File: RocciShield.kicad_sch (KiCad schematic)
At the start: 117 parts, among them J1 Battery, J2 M1, J3 M1, J4 M1, J5 M1, U1 DRV8871DDA, U2 TL7712A, U3 LMR33630CDDA, U4 DRV8871DDA, U5 DRV8871DDA, U6 DRV8871DDA, U7 TCA9548APWR, U8 AMS1117-3.3

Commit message: fixed issue #1 and some more things
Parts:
- removed C4: 22 µF, symbol Device:C
- removed D10: GR, symbol Device:LED
- removed R16: 430, symbol Device:R
- removed U2: TL7712A, symbol Power_Supervisor:TL7712A
- added C12, C18, C6: 100n, symbol Device:C
- added C4, C5: 22 µF, symbol Device:C_Polarized
- added D17: RED, symbol Device:LED
- added D6, D7, D8: GR, symbol Device:LED
- added F1, F11, F14, F17, F20, F23, F5, F8: 100 mA, symbol Device:Polyfuse
- added F26: 3A, symbol Device:Polyfuse
- added F27: 1A, symbol Device:Polyfuse
- added J11: I2C6, symbol Connector:Conn_01x04_Pin
- added J13: I2C7, symbol Connector:Conn_01x04_Pin
- added J14: Power, symbol Connector:Conn_01x04_Socket
- added J2: I2C0, symbol Connector:Conn_01x04_Pin
- added J3: I2C1, symbol Connector:Conn_01x04_Pin
- added J4: I2C2, symbol Connector:Conn_01x04_Pin
- added J5: I2C3, symbol Connector:Conn_01x04_Pin
- added J7: I2C4, symbol Connector:Conn_01x04_Pin
- added J9: I2C5, symbol Connector:Conn_01x04_Pin
- added Q1: IRF7416, symbol Device:Q_PMOS_GDS
- added R10: 383k 1%, symbol Device:R
- added R11: 10k, symbol Device:R
- added R12: 200, symbol Device:R
- added R13, R28: 20, symbol Device:R
- added R14: 1k, symbol Device:R
- added R15: 1k47 1%, symbol Device:R
- added R18: 14k3 1%, symbol Device:R
- added TP1, TP10, TP11, TP12, TP13, TP14, TP15, TP16, TP17, TP18, TP19, TP2, TP20, TP21, TP22, TP3, TP4, TP5, TP6, TP7, TP8, TP9: ~, symbol Connector:TestPoint
- added U3: L7808, symbol Regulator_Linear:L7808
- added U4: TPS3700, SOT95P280X110-6N, symbol TPS3700DDCR:TPS3700DDCR
- C11: value 22 µF -> 100n
- J10: renamed from J4; value M1 -> M3
- J12: renamed from J5; value M1 -> M4
- J8: renamed from J3; value M1 -> M2
- R21: renamed from R5; value 430 -> 1k
- R22: renamed from R6; value 430 -> 1k
- R26: renamed from R8; value 430 -> 1k
- R27: renamed from R9; value 430 -> 1k
- R32: renamed from R11; value 430 -> 1k
- R33: renamed from R12; value 430 -> 1k
- R37: renamed from R14; value 430 -> 1k
- R38: renamed from R15; value 430 -> 1k
- U1: renamed from U3; value LMR33630CDDA -> LMR33630
- U5: renamed from U7; value TCA9548APWR -> TCA9548A
- U6: renamed from U1; value DRV8871DDA -> DRV8871
- U7: renamed from U4; value DRV8871DDA -> DRV8871
- U8: renamed from U5; value DRV8871DDA -> DRV8871
- U9: renamed from U6; value DRV8871DDA -> DRV8871
- renumbered C14 to C10, C7 to C13, C6 to C14, C8 to C15, C9 to C16, C10 to C17, C5 to C3, C3 to C7, C13 to C8, C12 to C9, D11 to D1, D16 to D10, D17 to D11, D18 to D12, D3 to D13, D2 to D14, D19 to D15, D20 to D16, D4 to D18, D5 to D19, D12 to D2, D21 to D20, D22 to D21, D6 to D22, D7 to D23, D23 to D24, D24 to D25, D8 to D26, D9 to D27, D25 to D28, D26 to D29, D1 to D3, D13 to D4, D14 to D5, D15 to D9, F7 to F10, F8 to F12, F9 to F13, F10 to F15, F11 to F16, F12 to F18, F13 to F19, F1 to F2, F14 to F21, F15 to F22, F16 to F24, F17 to F25, F2 to F3, F3 to F4, F4 to F6, F5 to F7, F6 to F9, J2 to J6, JP4 to JP1, JP5 to JP2, JP6 to JP3, JP7 to JP4, JP3 to JP5, JP2 to JP6, JP1 to JP7, R20 to R1, R23 to R16, R24 to R17, R25 to R19, R19 to R2, R26 to R20, R4 to R23, R27 to R24, R28 to R25, R7 to R29, R2 to R3, R29 to R30, R30 to R31, R10 to R34, R31 to R35, R32 to R36, R13 to R39, R1 to R4, R33 to R40, R34 to R41, R3 to R5, R17 to R6, R18 to R7, R21 to R8, R22 to R9, U8 to U2
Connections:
- net +12V: now also C11.2, D8.2 (A), J14.1 (Pin_1), Q1.3 (S), U3.1 (IN)
- net +3V3: now also D7.2 (A), F27.1, TP11.1
- net +5V: now also JP5.3 (B), JP6.3 (B), JP7.3 (B), U5.24 (VCC), C4.1, C5.1, C6.2, D6.2 (A), F26.1, TP3.1; no longer C11.1
- net GND: now also C11.1, XA1.GND1 (GND), XA1.GND2 (GND), XA1.GND3 (GND), XA1.GND5 (GND), XA1.GND6 (GND), C12.1, C18.1, C6.1, J11.1 (Pin_1), J13.1 (Pin_1), J14.4 (Pin_4), J2.1 (Pin_1), J3.1 (Pin_1), J4.1 (Pin_1), J5.1 (Pin_1), J7.1 (Pin_1), J9.1 (Pin_1), R12.2, R13.2, R14.2, R18.2, R28.2, U3.2 (GND), U4.2 (GND)
- net I2C_SCL: now also XA1.D21 (D21/SCL), TP8.1
- net I2C_SDA: now also XA1.D20 (D20/SDA), TP9.1
- net M1_IN1: now also XA1.D4, TP15.1; no longer U7.3 (IN1), U8.3 (IN1), U9.3 (IN1)
- net M1_IN2: now also XA1.D3 (D3_INT1), TP16.1; no longer U7.2 (IN2), U8.2 (IN2), U9.2 (IN2)
- net M2_2: now reaches D18.2 (A), D19.1 (K), J8.1 (Pin_1), U7.8 (OUT2)
- net M2_1: now reaches J8.2 (Pin_2), R26.1, R27.1, U7.6 (OUT1)
- net M3_2: now reaches D26.2 (A), D27.1 (K), J12.1 (Pin_1), U9.8 (OUT2)
- net M3_2: now also D22.2 (A), D23.1 (K), J10.1 (Pin_1), U8.8 (OUT2)
- net at JP11.2 (C), R40.1, R41.1: now also F23.1
- net at JP3.2 (C), R16.1, R17.1: now also F8.1
- net M3_1: now reaches J10.2 (Pin_2), R32.1, R33.1, U8.6 (OUT1)
- net M3_1: now also J12.2 (Pin_2), R37.1, R38.1, U9.6 (OUT1)
- net at JP10.2 (C), R35.1, R36.1: now also F20.1
- net at JP2.2 (C), R8.1, R9.1: now also F5.1
- net 12V_input: now reaches F2.1, J1.2 (Pin_2)
- net 12V_after_fuse: now reaches D3.1 (K), F2.2
- net 12V_after_fuse: now also Q1.2 (D), R10.1, R11.1, TP7.1, U4.5 (VDD)
- net at JP8.2 (C), R24.1, R25.1: now also F14.1
- net M1_1: now reaches J6.2 (Pin_2), R21.1, R22.1, U6.6 (OUT1)
- net M1_2: now reaches D13.2 (A), D14.1 (K), J6.1 (Pin_1), U6.8 (OUT2)
- net SW: now reaches C3.1, L1.1, U1.8 (SW)
- net SW: now also TP2.1
- net Boot: now reaches C3.2, U1.7 (BOOT)
- net Boot: now also TP1.1
- net FB: now reaches R3.2, R5.1, U1.5 (FB)
- net FB: now also C4.2, C5.2, TP5.1; no longer C11.2
- net at JP1.2 (C), R1.1, R2.1: now also F1.1
- net at JP9.2 (C), R30.1, R31.1: now also F17.1
- net at C7.1, R4.1, U1.6 (VCC): now also TP4.1
- net PG: now reaches R4.2, U1.4 (PG)
- net PG: now also TP6.1
- net at JP4.2 (C), R19.1, R20.1: now also F11.1
- net ADC_BAT: now reaches XA1.A0
- net ADC_BAT: now also R10.2, R15.1, U4.3 (INA+)
- net M4_IN1: now reaches XA1.D10
- net M4_IN1: now also U9.3 (IN1), TP21.1
- net ERROR_LED: now reaches XA1.D2 (D2_INT0)
- net ERROR_LED: now also D17.2 (A)
- net M2_IN2: now reaches XA1.D5
- net M2_IN2: now also U7.2 (IN2), TP18.1
- net M2_IN1: now reaches XA1.D6
- net M2_IN1: now also U7.3 (IN1), TP17.1
- net M3_IN2: now reaches XA1.D7
- net M3_IN2: now also U8.2 (IN2), TP20.1
- net M3_IN1: now reaches XA1.D8
- net M3_IN1: now also U8.3 (IN1), TP19.1
- net M4_IN2: now reaches XA1.D9
- net M4_IN2: now also U9.2 (IN2), TP22.1
- net IOREF: now reaches XA1.IORF (IOREF)
- net IOREF: now also R6.1, R7.1
- net +8V: now reaches XA1.VIN
- net +8V: now also C12.2, C18.2, TP12.1, U3.3 (OUT)
- net SCL0: no longer names the net of F3.2
- net SCL0: now also J2.3 (Pin_3)
- net SCL1: no longer names the net of F6.2
- net SCL1: now also J3.3 (Pin_3)
- net SCL2: no longer names the net of F9.2
- net SCL2: now also J4.3 (Pin_3)
- net SCL3: no longer names the net of F12.2
- net SCL3: now also J5.3 (Pin_3)
- net SCL4: no longer names the net of F15.2
- net SCL4: now also J7.3 (Pin_3)
- net SCL5: no longer names the net of F18.2
- net SCL5: now also J9.3 (Pin_3)
- net SCL6: no longer names the net of F21.2
- net SCL6: now also J11.3 (Pin_3)
- net SCL7: no longer names the net of F24.2
- net SCL7: now also J13.3 (Pin_3)
- net SDA0: no longer names the net of F4.2
- net SDA0: now also J2.2 (Pin_2)
- net SDA1: no longer names the net of F7.2
- net SDA1: now also J3.2 (Pin_2)
- net SDA2: no longer names the net of F10.2
- net SDA2: now also J4.2 (Pin_2)
- net SDA3: no longer names the net of F13.2
- net SDA3: now also J5.2 (Pin_2)
- net SDA4: no longer names the net of F16.2
- net SDA4: now also J7.2 (Pin_2)
- net SDA5: no longer names the net of F19.2
- net SDA5: now also J9.2 (Pin_2)
- net SDA6: no longer names the net of F22.2
- net SDA6: now also J11.2 (Pin_2)
- net SDA7: no longer names the net of F25.2
- net SDA7: now also J13.2 (Pin_2)
- removed net VCC: JP5.3 (B), JP6.3 (B), JP7.3 (B), R6.1, R7.1, U5.24 (VCC)
- new net: Q1.1 (G), R11.2, TP13.1, U4.6 (OUTB)
- new net: F26.2, J14.2 (Pin_2)
- new net: F27.2, J14.3 (Pin_3)
- new net: D6.1 (K), R12.1
- new net: TP10.1, U4.1 (OUTA)
- new net: R15.2, R18.1, TP14.1, U4.4 (INB-)
- new net: F23.2, J13.4 (Pin_4)
- new net: D17.1 (K), R28.1
- new net: F1.2, J2.4 (Pin_4)
- new net: D7.1 (K), R13.1
- new net: F11.2, J5.4 (Pin_4)
- new net: F8.2, J4.4 (Pin_4)
- new net: F20.2, J11.4 (Pin_4)
- new net: F14.2, J7.4 (Pin_4)
- new net: D8.1 (K), R14.1
- new net: F5.2, J3.4 (Pin_4)
- new net: F17.2, J9.4 (Pin_4)
- no-connect marks 0 -> 72
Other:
- note added: "Error LED"
- note added: "Power Connector"
- note added: "TODO: - verify limit resistor of LEDs - specify components for switching regulator - double check 100 mA poly fuse for I2C VCC - define netclasses - define footprints - is the power connector large enough?"
- note added: "at 10,8 V it turns off at 11 V it turns on again"
- note removed: "ICL7665 von 1.6 bis 16V mit 3uA bei 1.3V Referenz für overvoltage und undervoltage, einstellbare Hysterese, open drain. MIC841 von 1.5 bis 5.5V mit 1.5uA bei 1.24V Referenz und einstellbarer Hysterese. MAX921=LTC1440 von 2 bis 11V mit 2.1uA bei 1.18V Referenz mit einstellbarer Hysterese MAX16010-MAX16014 von 5.5 bis 72V bei 25uA mit 1.23V Referenz, Hysterese und UVLO, MCP65R41 (push pull) MCP65R4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"
- company: (none) -> RoCCI e.V.
- title: (none) -> RoCCI Shield
- moved on the sheet: C1, C10, C13, C14, C15, C16, C17, C2, C3, C7, C8, C9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

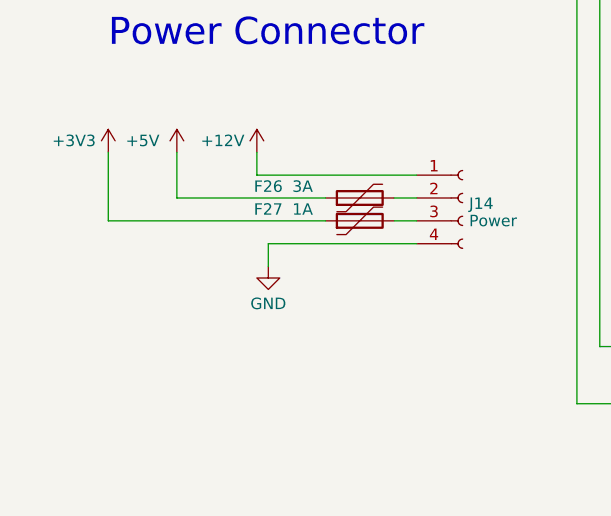
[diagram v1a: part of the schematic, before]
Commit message: added zener diode
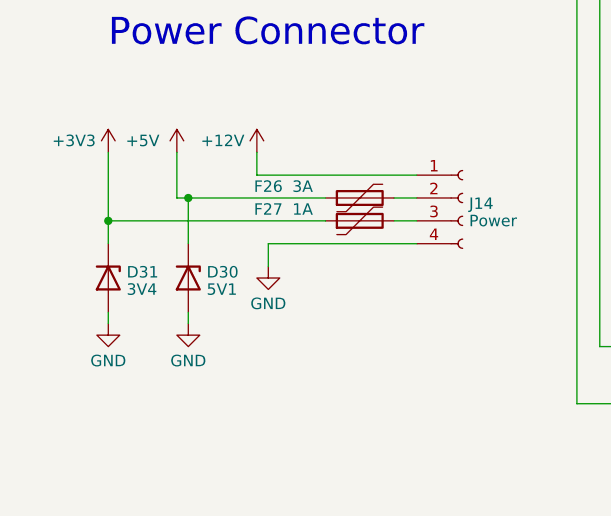
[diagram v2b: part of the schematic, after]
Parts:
- added D30: 5V1, symbol Device:D_Zener
- added D31: 3V4, symbol Device:D_Zener
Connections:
- net +3V3: now also D31.1 (K)
- net +5V: now also D30.1 (K)
- net GND: now also D30.2 (A), D31.2 (A)
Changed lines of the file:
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@@
     (title "RoCCI Shield")
     (date "2023-06-23")
-    (rev "0.1")
+    (rev "0.2")
     (company "RoCCI e.V.")
   )
@@
   (junction (at 113.03 168.91) (diameter 0) (color 0 0 0 0)
   )
+  (junction (at 25.4 234.95) (diameter 0) (color 0 0 0 0)
+  )
   (junction (at 355.6 158.75) (diameter 0) (color 0 0 0 0)
   )
@@
   (junction (at 361.95 48.26) (diameter 0) (color 0 0 0 0)
   )
+  (junction (at 34.29 232.41) (diameter 0) (color 0 0 0 0)
+  )
   (junction (at 363.22 224.79) (diameter 0) (color 0 0 0 0)
   )
@@
     (stroke (width 0) (type default))
   )
-  (wire (pts (xy 49.53 232.41) (xy 33.02 232.41))
+  (wire (pts (xy 49.53 232.41) (xy 34.29 232.41))
     (stroke (width 0) (type default))
   )
@@
     (stroke (width 0) (type default))
   )
+  (wire (pts (xy 25.4 245.11) (xy 25.4 246.38))
+    (stroke (width 0) (type default))
+  )
   (wire (pts (xy 132.08 73.66) (xy 119.38 73.66))
     (stroke (width 0) (type default))
@@
     (stroke (width 0) (type default))
   )
+  (wire (pts (xy 34.29 232.41) (xy 33.02 232.41))
+    (stroke (width 0) (type default))
+  )
   (wire (pts (xy 177.8 71.12) (xy 170.18 71.12))
     (stroke (width 0) (type default))
@@
     (stroke (width 0) (type default))
   )
+  (wire (pts (xy 34.29 245.11) (xy 34.29 246.38))
+    (stroke (width 0) (type default))
+  )
   (wire (pts (xy 341.63 83.82) (xy 351.79 83.82))
     (stroke (width 0) (type default))
@@
     (stroke (width 0) (type default))
   )
+  (wire (pts (xy 34.29 232.41) (xy 34.29 237.49))
+    (stroke (width 0) (type default))
+  )
   (wire (pts (xy 355.6 146.05) (xy 355.6 148.59))
     (stroke (width 0) (type default))
@@
     (stroke (width 0) (type default))
   )
+  (wire (pts (xy 25.4 234.95) (xy 25.4 237.49))
+    (stroke (width 0) (type default))
+  )
   (wire (pts (xy 88.9 101.6) (xy 88.9 198.12))
     (stroke (width 0) (type default))
@@
     )
   )
+  (symbol (lib_id "power:GND") (at 25.4 246.38 0) (unit 1)
+    (in_bom yes) (on_board yes) (dnp no) (fields_autoplaced)
+    (property "Reference" "#PWR0109" (at 25.4 252.73 0)
+      (effects (font (size 1.27 1.27)) hide)
+    )
+    (property "Value" "GND" (at 25.4 250.5155 0)
+      (effects (font (size 1.27 1.27)))
+    )
+    (property "Footprint" "" (at 25.4 246.38 0)
+      (effects (font (size 1.27 1.27)) hide)
+    )
+    (property "Datasheet" "" (at 25.4 246.38 0)
+      (effects (font (size 1.27 1.27)) hide)
+    )
+    (pin "1")
+    (instances
+      (project "RocciShield"
+        (path "/0431e819-1fd6-4448-bdea-d8b652bd339c"
+          (reference "#PWR0109") (unit 1)
+        )
+      )
+    )
+  )
   (symbol (lib_id "Device:Polyfuse") (at 151.13 73.66 90) (unit 1)
     (in_bom yes) (on_board yes) (dnp no)
@@
     )
   )
+  (symbol (lib_id "Device:D_Zener") (at 34.29 241.3 270) (unit 1)
+    (in_bom yes) (on_board yes) (dnp no) (fields_autoplaced)
+    (property "Reference" "D30" (at 36.322 240.6563 90)
+      (effects (font (size 1.27 1.27)) (justify left))
+    )
+    (property "Value" "5V1" (at 36.322 242.5773 90)
+      (effects (font (size 1.27 1.27)) (justify left))
+    )
+    (property "Footprint" "" (at 34.29 241.3 0)
+      (effects (font (size 1.27 1.27)) hide)
+    )
+    (property "Datasheet" "~" (at 34.29 241.3 0)
+      (effects (font (size 1.27 1.27)) hide)
+    )
+    (pin "1")
+    (pin "2")
+    (instances
+      (project "RocciShield"
+        (path "/0431e819-1fd6-4448-bdea-d8b652bd339c"
+          (reference "D30") (unit 1)
+        )
+      )
+    )
+  )
   (symbol (lib_id "Device:R") (at 43.18 67.31 0) (unit 1)
     (in_bom yes) (on_board yes) (dnp no) (fields_autoplaced)
@@
     )
   )
+  (symbol (lib_id "Device:D_Zener") (at 25.4 241.3 270) (unit 1)
+    (in_bom yes) (on_board yes) (dnp no) (fields_autoplaced)
+    (property "Reference" "D31" (at 27.432 240.6563 90)
+      (effects (font (size 1.27 1.27)) (justify left))
+    )
+    (property "Value" "3V4" (at 27.432 242.5773 90)
+      (effects (font (size 1.27 1.27)) (justify left))
+    )
+    (property "Footprint" "" (at 25.4 241.3 0)
+      (effects (font (size 1.27 1.27)) hide)
+    )
+    (property "Datasheet" "~" (at 25.4 241.3 0)
+      (effects (font (size 1.27 1.27)) hide)
+    )
+    (pin "1")
+    (pin "2")
+    (instances
+      (project "RocciShield"
+        (path "/0431e819-1fd6-4448-bdea-d8b652bd339c"
+          (reference "D31") (unit 1)
+        )
+      )
+    )
+  )
   (symbol (lib_id "Connector:Conn_01x04_Pin") (at 181.61 165.1 180) (unit 1)
     (in_bom yes) (on_board yes) (dnp no) (fields_autoplaced)
@@
         )
       )
+    )
+  )
+  (symbol (lib_id "power:GND") (at 34.29 246.38 0) (unit 1)
+    (in_bom yes) (on_board yes) (dnp no) (fields_autoplaced)
+    (property "Reference" "#PWR0108" (at 34.29 252.73 0)
+      (effects (font (size 1.27 1.27)) hide)
+    )
+    (property "Value" "GND" (at 34.29 250.5155 0)
+      (effects (font (size 1.27 1.27)))
+    )
+    (property "Footprint" "" (at 34.29 246.38 0)
+      (effects (font (size 1.27 1.27)) hide)
+    )
+    (property "Datasheet" "" (at 34.29 246.38 0)
+      (effects (font (size 1.27 1.27)) hide)
+    )
+    (pin "1")
+    (instances
+      (project "RocciShield"
+        (path "/0431e819-1fd6-4448-bdea-d8b652bd339c"
+          (reference "#PWR0108") (unit 1)
+        )
+      )
